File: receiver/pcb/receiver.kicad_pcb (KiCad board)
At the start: 2 copper layers, 39 x 43.2 mm, 28 parts, among them J4 Conn_01x01_Female-weapon, J5 Conn_01x01_Female-weapon, M1 Conn_01x02_Female, M2 Conn_01x02_Female, U1 DRV8870DDA, U2 DRV8870DDA, U3 AMS1117-3.3, U4 ESP32-C3-MINI-1

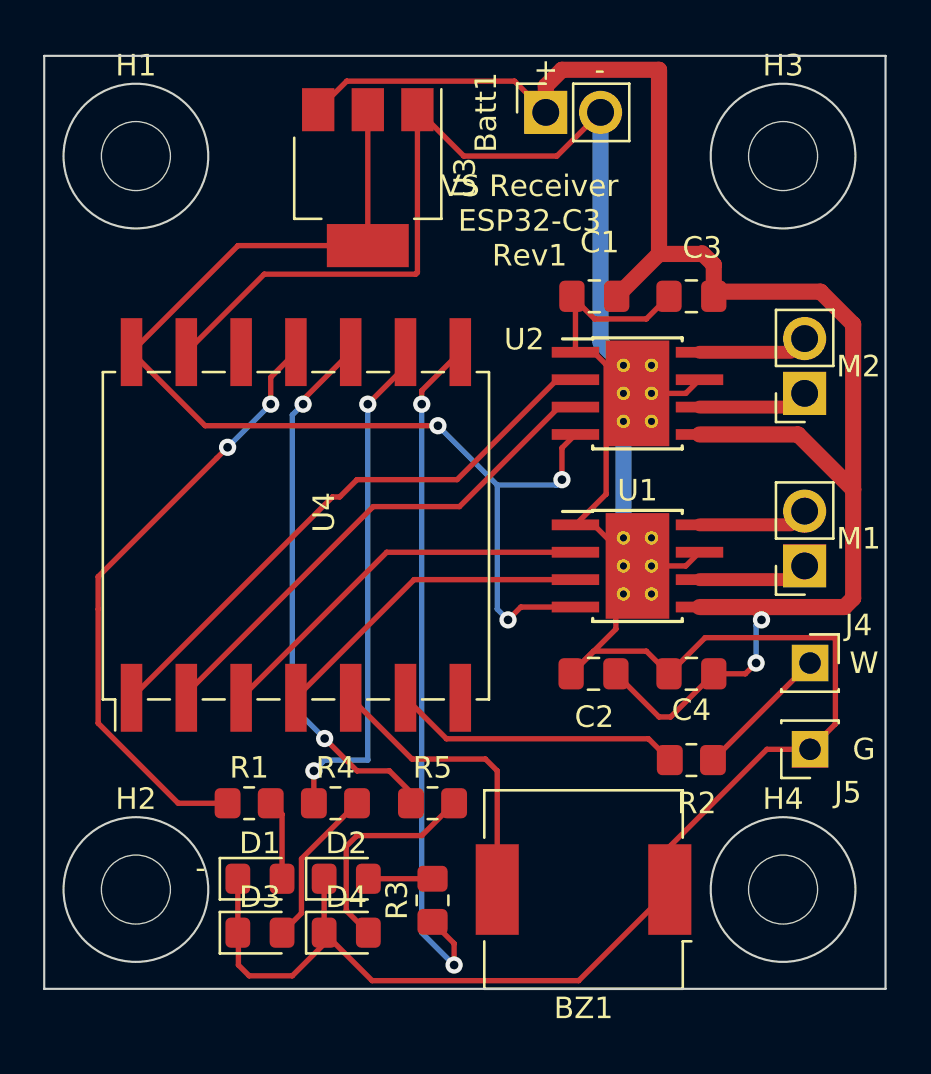
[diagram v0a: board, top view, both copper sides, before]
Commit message: added footprints library
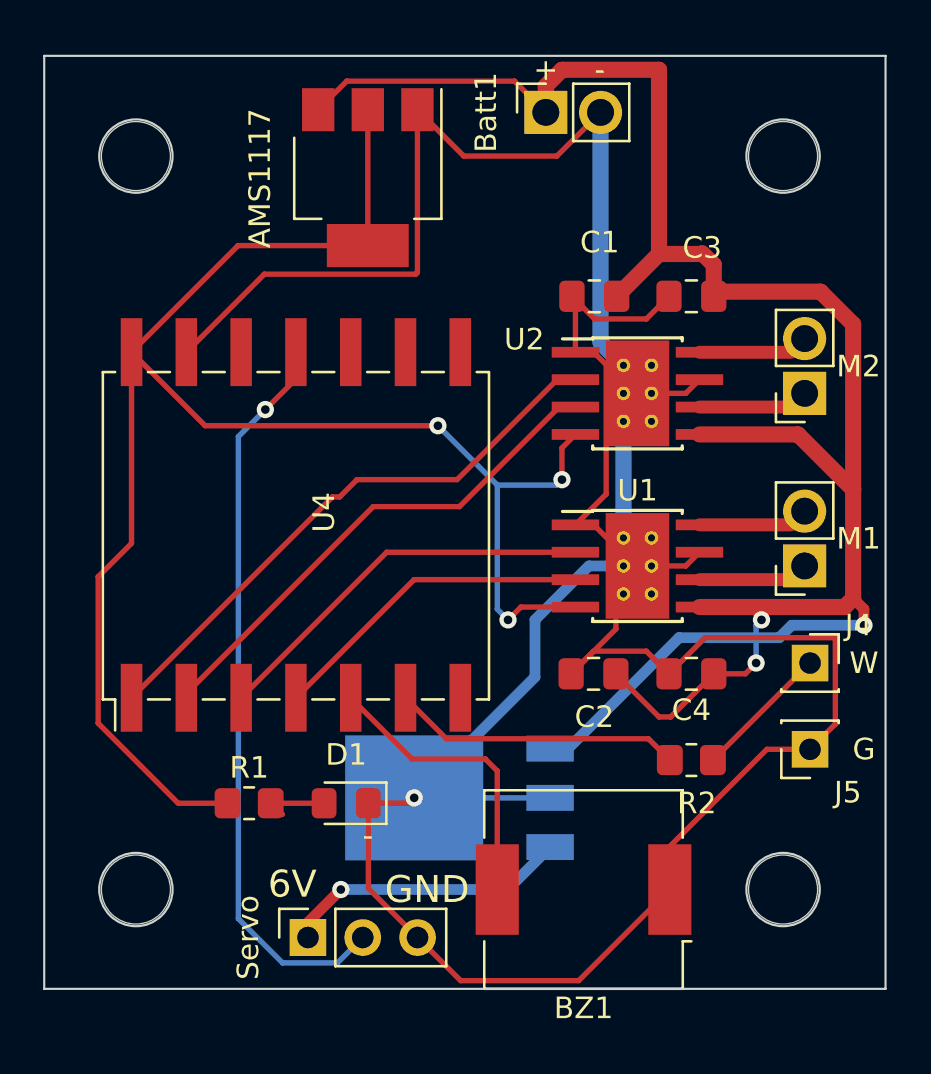
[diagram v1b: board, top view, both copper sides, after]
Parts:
- removed D2, D3, D4: LED, LED_SMD:LED_0805_2012Metric_Pad1.15x1.40mm_HandSolder
- removed R3, R4, R5: 680 ohm, Resistor_SMD:R_0805_2012Metric_Pad1.20x1.40mm_HandSolder
- added L7806: L7806, Package_TO_SOT_SMD:TO-252-3_TabPin2, B.Cu at (165.8, 110.8)
- added Servo: Servo, Connector_PinSocket_2.54mm:PinSocket_1x03_P2.54mm_Vertical, F.Cu at (158.7, 117.2)
- moved D1 5.32 mm to (160.5, 111.0), turned to 180 degrees
- moved G*** 2.25 mm to (166.0, 96.8)
- renumbered U3 to AMS1117
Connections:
- R1 pad 1: /LED1 -> +3V3
- U4 pad 16: /LED1 -> /Servo
- U4 pad 21: /LED2 -> unconnected-(U4-Pad21)
- U4 pad 22: /LED3 -> unconnected-(U4-Pad22)
- U4 pad 23: /LED4 -> unconnected-(U4-Pad23)
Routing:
- net /Servo: track 0.00 -> 34.5 mm, vias 0 -> 1
- net /LED2: track 32.2 -> 0.00 mm, vias 2 -> 0
- net /LED1: track 28.5 -> 0.00 mm, vias 2 -> 0
- net +3V3: track 54.1 -> 79.5 mm
- net /LED4: track 25.2 -> 0.00 mm, vias 2 -> 0
- net /LED3: track 23.8 -> 0.00 mm, vias 2 -> 0
- net +12V: track 83.0 -> 101.0 mm, vias 2 -> 3
- net GND: track 139.7 -> 155.5 mm, vias 0 -> 1
- net +6V: track 0.00 -> 13.4 mm, vias 0 -> 1
- net Net-(D4-Pad2): track 10.3 -> 0.00 mm
- net Net-(D3-Pad2): track 7.44 -> 0.00 mm
- net Net-(D2-Pad2): track 2.97 -> 0.00 mm
- net Net-(D1-Pad2): track 3.75 -> 3.25 mm
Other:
- outline, holes or cut-outs redrawn
- board text added: "6V"
- board text added: "GND"

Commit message: minor silkscreen mod on receiver
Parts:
- renumbered R1 to 680, U4 to ESP32-C3, D1 to PWR
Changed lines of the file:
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@@
     (property "Sheetname" "")
     (attr smd)
-    (fp_text reference "U4" (at 0 -0.5 90 unlocked) (layer "F.SilkS")
+    (fp_text reference "ESP32-C3" (at 0 -0.5 90 unlocked) (layer "F.SilkS")
       (effects (font (size 1 1) (thickness 0.15)))
     )
@@
     (property "Sheetname" "")
     (attr smd)
-    (fp_text reference "R1" (at 0 -1.65) (layer "F.SilkS")
+    (fp_text reference "680" (at 0 -1.65) (layer "F.SilkS")
       (effects (font (size 1 1) (thickness 0.15)))
     )
@@
     (property "Sheetname" "")
     (attr smd)
-    (fp_text reference "D1" (at 0 2.25) (layer "F.SilkS")
+    (fp_text reference "PWR" (at 0 2.25) (layer "F.SilkS")
       (effects (font (size 1 1) (thickness 0.15)))
     )
@@
       ) (layer "B.SilkS") (width 0) (fill solid))
   )
+  (gr_rect (start 147.5 94.5) (end 152 101.5) (layer "F.SilkS") (width 0.15) (fill none))
   (gr_rect (start 150.75 81) (end 180.75 115) (layer "Dwgs.User") (width 0.15) (fill none))
   (gr_circle (center 150.75 115) (end 152.45 115) (layer "Edge.Cuts") (width 0.1) (fill none))

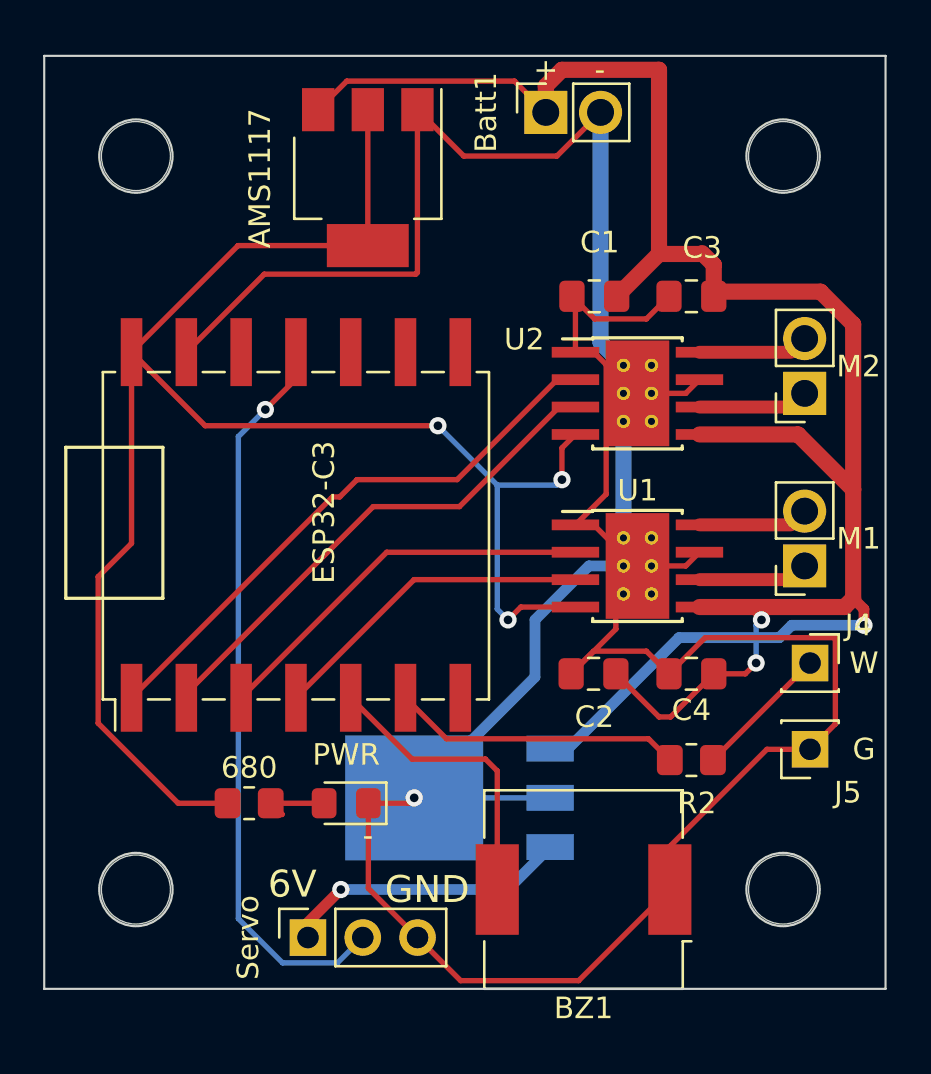
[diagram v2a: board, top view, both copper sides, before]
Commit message: change ESC connection to 3pin header
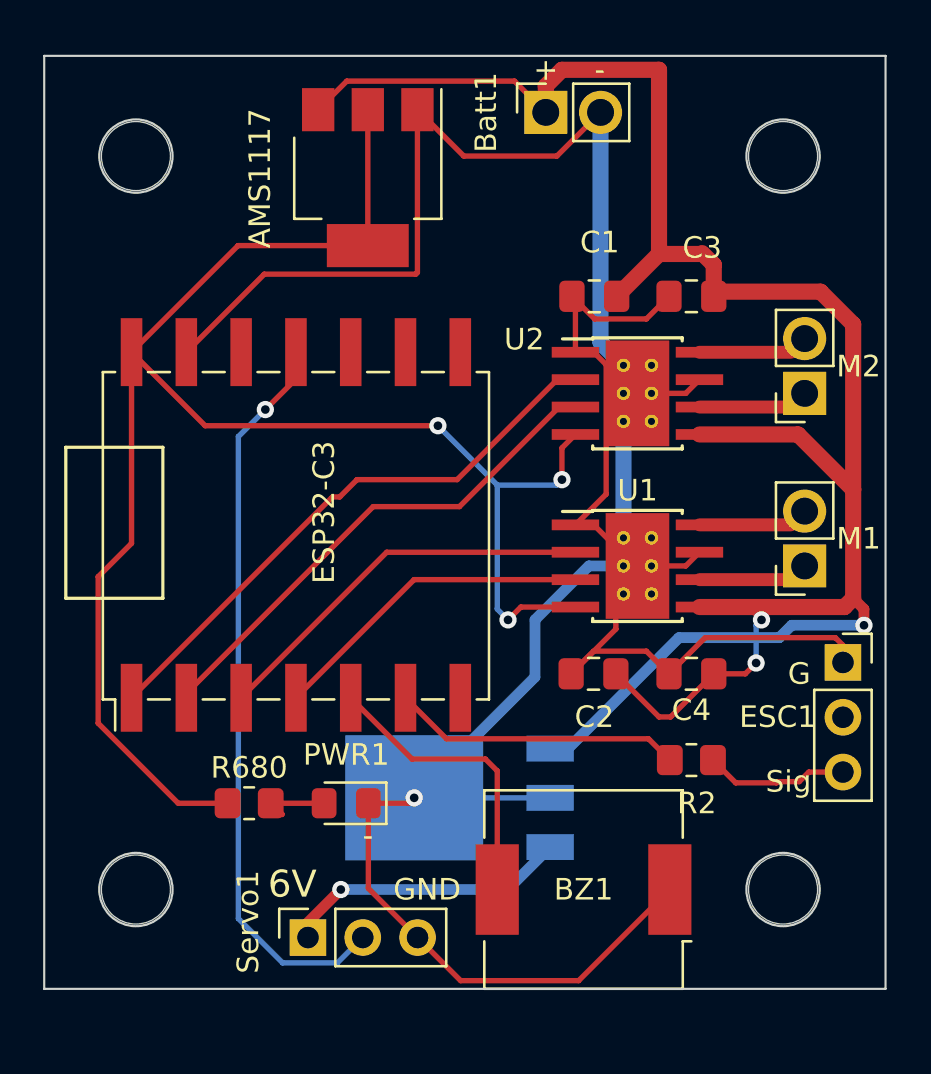
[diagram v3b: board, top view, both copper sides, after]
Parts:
- removed J4, J5: Conn_01x01_Female-weapon, Connector_PinSocket_2.54mm:PinSocket_1x01_P2.54mm_Vertical
- added ESC1: ESC, Connector_PinSocket_2.54mm:PinSocket_1x03_P2.54mm_Vertical, F.Cu at (183.5, 104.5)
- renumbered PWR to PWR1, 680 to R680, Servo to Servo1
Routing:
- net GND: track 155.5 -> 140.7 mm
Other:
- board text added: "Sig"
- board text removed: "W"
